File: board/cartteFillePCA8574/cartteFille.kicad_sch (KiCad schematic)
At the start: 13 parts, among them U1 LM358, U201 PCA8574D,518, U202 PCA8574D,518

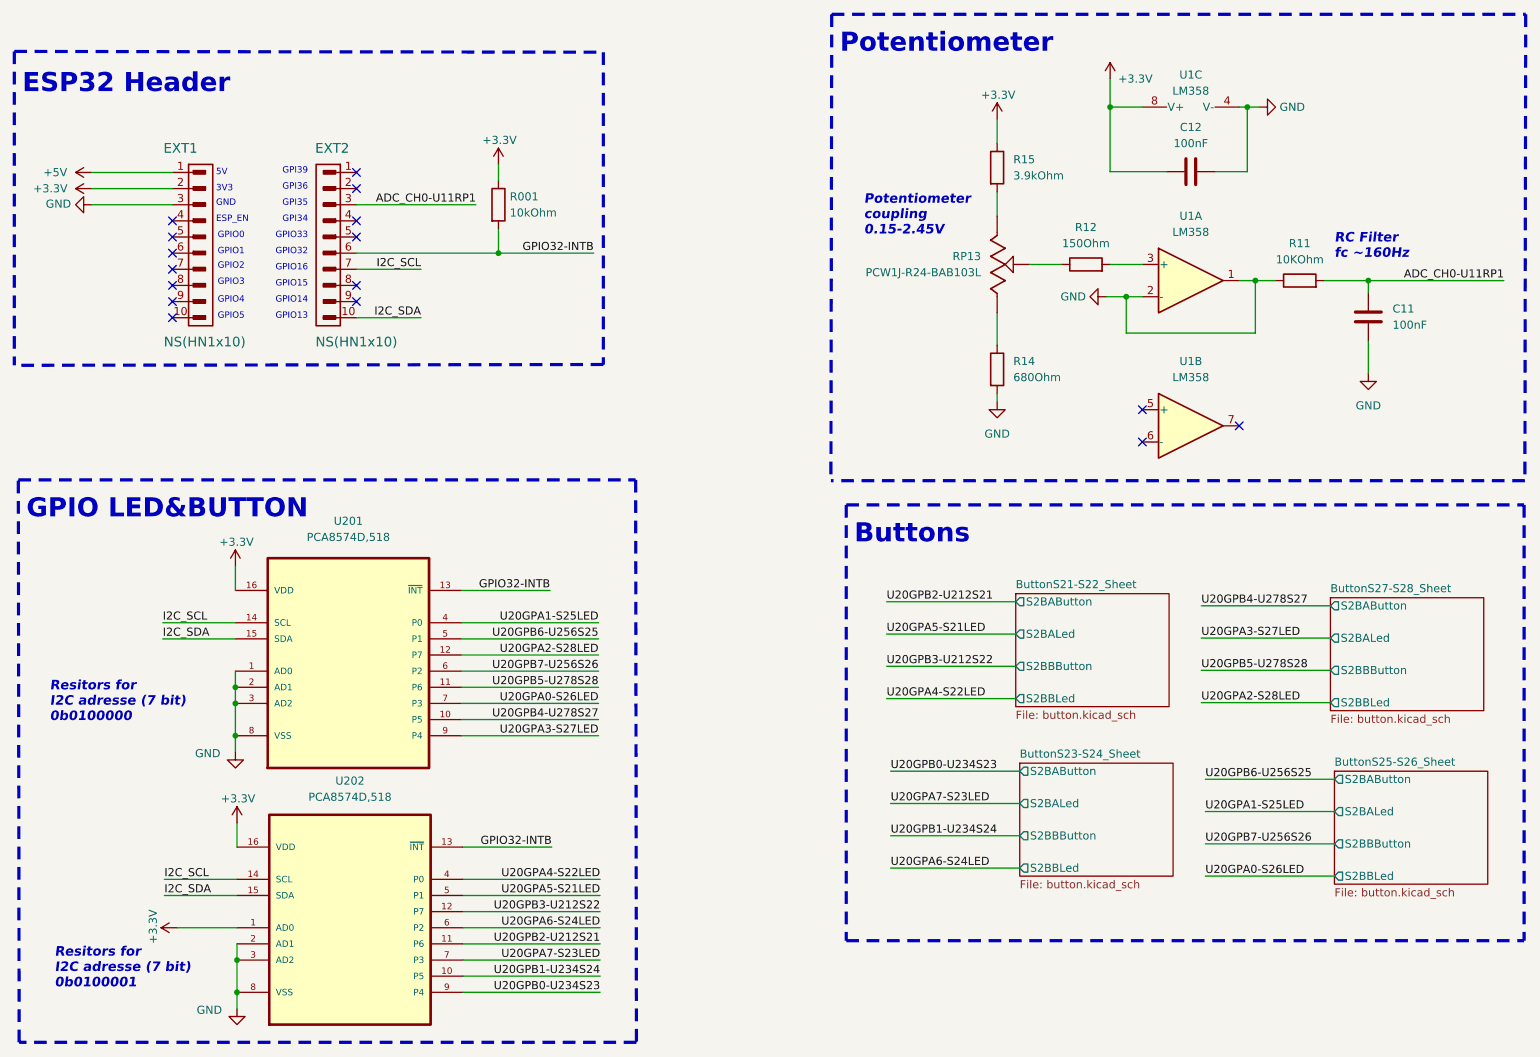
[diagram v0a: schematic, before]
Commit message: Review_GPIO_Replaced
version avant la review du pcb avec les nouveau gpio
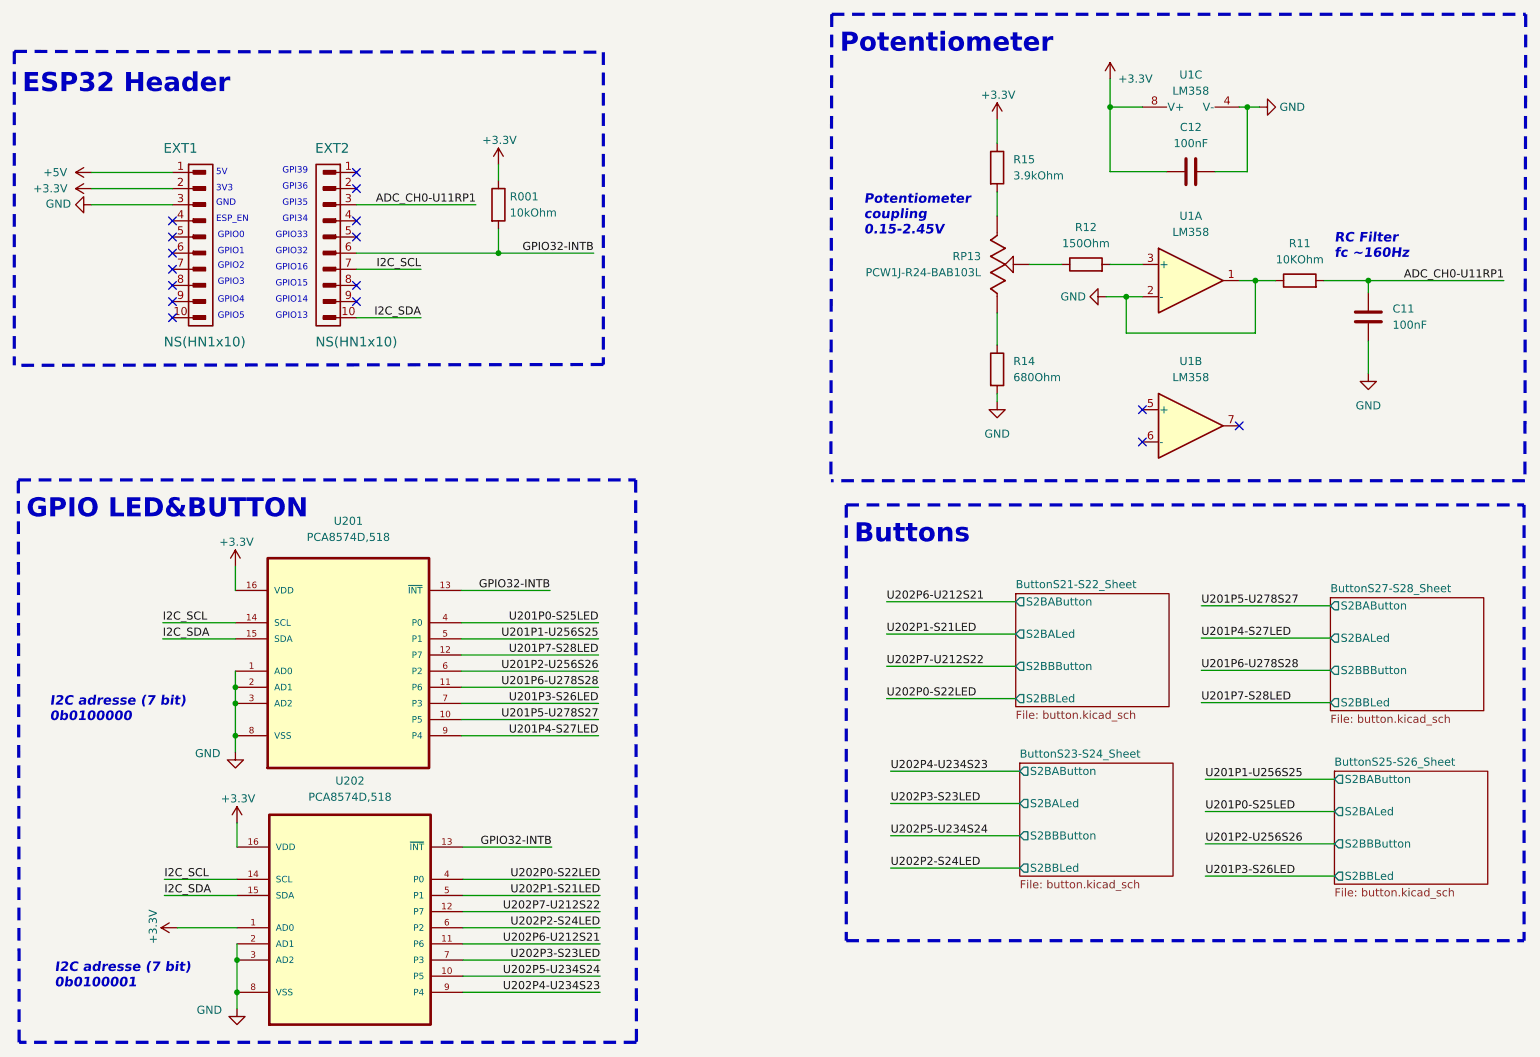
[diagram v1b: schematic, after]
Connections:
- net U20GPA0-S26LED renamed U201P3-S26LED
- net U20GPA1-S25LED renamed U201P0-S25LED
- net U20GPA2-S28LED renamed U201P7-S28LED
- net U20GPA3-S27LED renamed U201P4-S27LED
- net U20GPA4-S22LED renamed U202P0-S22LED
- net U20GPA5-S21LED renamed U202P1-S21LED
- net U20GPA6-S24LED renamed U202P2-S24LED
- net U20GPA7-S23LED renamed U202P3-S23LED
- net U20GPB0-U234S23 renamed U202P4-U234S23
- net U20GPB1-U234S24 renamed U202P5-U234S24
- net U20GPB2-U212S21 renamed U202P6-U212S21
- net U20GPB3-U212S22 renamed U202P7-U212S22
- net U20GPB4-U278S27 renamed U201P5-U278S27
- net U20GPB5-U278S28 renamed U201P6-U278S28
- net U20GPB6-U256S25 renamed U201P1-U256S25
- net U20GPB7-U256S26 renamed U201P2-U256S26
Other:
- note added: "I2C adresse (7 bit) 0b0100000"
- note added: "I2C adresse (7 bit) 0b0100001"
- note removed: "Resitors for I2C adresse (7 bit) 0b0100000"
- note removed: "Resitors for I2C adresse (7 bit) 0b0100001"
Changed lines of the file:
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@@
     (effects (font (size 3 3) (thickness 0.6) bold) (justify left bottom))
   )
-  (text "Resitors for\nI2C adresse (7 bit)\n0b0100000" (at 39.116 128.778 0)
+  (text "I2C adresse (7 bit)\n0b0100000" (at 39.116 128.778 0)
     (effects (font (size 1.5 1.5) (thickness 0.3) bold italic) (justify left bottom))
   )
@@
     (effects (font (size 1 1)) (justify left bottom))
   )
-  (text "Resitors for\nI2C adresse (7 bit)\n0b0100001" (at 39.878 170.688 0)
+  (text "I2C adresse (7 bit)\n0b0100001" (at 39.878 170.688 0)
     (effects (font (size 1.5 1.5) (thickness 0.3) bold italic) (justify left bottom))
   )
@@
     (effects (font (size 1 1)) (justify right bottom))
   )
-  (label "U20GPB5-U278S28" (at 125.476 123.19 180)
+  (label "U201P6-U278S28" (at 125.476 123.19 180)
     (effects (font (size 1.27 1.27)) (justify right bottom))
   )
@@
     (effects (font (size 1.27 1.27)) (justify right bottom))
   )
-  (label "U20GPB0-U234S23" (at 125.73 171.196 180)
+  (label "U202P4-U234S23" (at 125.73 171.196 180)
     (effects (font (size 1.27 1.27)) (justify right bottom))
   )
@@
     (effects (font (size 1.27 1.27)) (justify right bottom))
   )
-  (label "U20GPB7-U256S26" (at 220.98 147.828 0)
+  (label "U201P2-U256S26" (at 220.98 147.828 0)
     (effects (font (size 1.27 1.27)) (justify left bottom))
   )
@@
     (effects (font (size 1.27 1.27)) (justify right bottom))
   )
-  (label "U20GPA4-S22LED" (at 170.815 124.968 0)
+  (label "U202P0-S22LED" (at 170.815 124.968 0)
     (effects (font (size 1.27 1.27)) (justify left bottom))
   )
-  (label "U20GPB4-U278S27" (at 125.476 128.27 180)
+  (label "U201P5-U278S27" (at 125.476 128.27 180)
     (effects (font (size 1.27 1.27)) (justify right bottom))
   )
-  (label "U20GPB4-U278S27" (at 220.345 110.363 0)
+  (label "U201P5-U278S27" (at 220.345 110.363 0)
     (effects (font (size 1.27 1.27)) (justify left bottom))
   )
@@
     (effects (font (size 1.27 1.27)) (justify right bottom))
   )
-  (label "U20GPA7-S23LED" (at 171.45 141.478 0)
+  (label "U202P3-S23LED" (at 171.45 141.478 0)
     (effects (font (size 1.27 1.27)) (justify left bottom))
   )
-  (label "U20GPB1-U234S24" (at 125.73 168.656 180)
+  (label "U202P5-U234S24" (at 125.73 168.656 180)
     (effects (font (size 1.27 1.27)) (justify right bottom))
   )
-  (label "U20GPA1-S25LED" (at 125.476 113.03 180)
+  (label "U201P0-S25LED" (at 125.476 113.03 180)
     (effects (font (size 1.27 1.27)) (justify right bottom))
   )
@@
     (effects (font (size 1.27 1.27)) (justify left bottom))
   )
-  (label "U20GPB7-U256S26" (at 125.476 120.65 180)
+  (label "U201P2-U256S26" (at 125.476 120.65 180)
     (effects (font (size 1.27 1.27)) (justify right bottom))
   )
-  (label "U20GPB1-U234S24" (at 171.45 146.558 0)
+  (label "U202P5-U234S24" (at 171.45 146.558 0)
     (effects (font (size 1.27 1.27)) (justify left bottom))
   )
-  (label "U20GPA0-S26LED" (at 125.476 125.73 180)
+  (label "U201P3-S26LED" (at 125.476 125.73 180)
     (effects (font (size 1.27 1.27)) (justify right bottom))
   )
-  (label "U20GPB5-U278S28" (at 220.345 120.523 0)
+  (label "U201P6-U278S28" (at 220.345 120.523 0)
     (effects (font (size 1.27 1.27)) (justify left bottom))
   )
-  (label "U20GPA3-S27LED" (at 125.476 130.81 180)
+  (label "U201P4-S27LED" (at 125.476 130.81 180)
     (effects (font (size 1.27 1.27)) (justify right bottom))
   )
-  (label "U20GPA0-S26LED" (at 220.98 152.908 0)
+  (label "U201P3-S26LED" (at 220.98 152.908 0)
     (effects (font (size 1.27 1.27)) (justify left bottom))
   )
@@
     (effects (font (size 1.27 1.27)) (justify left bottom))
   )
-  (label "U20GPB6-U256S25" (at 220.98 137.668 0)
+  (label "U201P1-U256S25" (at 220.98 137.668 0)
     (effects (font (size 1.27 1.27)) (justify left bottom))
   )
-  (label "U20GPA7-S23LED" (at 125.73 166.116 180)
+  (label "U202P3-S23LED" (at 125.73 166.116 180)
     (effects (font (size 1.27 1.27)) (justify right bottom))
   )
-  (label "U20GPA2-S28LED" (at 220.345 125.603 0)
+  (label "U201P7-S28LED" (at 220.345 125.603 0)
     (effects (font (size 1.27 1.27)) (justify left bottom))
   )
-  (label "U20GPB6-U256S25" (at 125.476 115.57 180)
+  (label "U201P1-U256S25" (at 125.476 115.57 180)
     (effects (font (size 1.27 1.27)) (justify right bottom))
   )
-  (label "U20GPA1-S25LED" (at 220.98 142.748 0)
+  (label "U201P0-S25LED" (at 220.98 142.748 0)
     (effects (font (size 1.27 1.27)) (justify left bottom))
   )
-  (label "U20GPA5-S21LED" (at 170.815 114.808 0)
+  (label "U202P1-S21LED" (at 170.815 114.808 0)
     (effects (font (size 1.27 1.27)) (justify left bottom))
   )
-  (label "U20GPB3-U212S22" (at 125.73 158.496 180)
+  (label "U202P7-U212S22" (at 125.73 158.496 180)
     (effects (font (size 1.27 1.27)) (justify right bottom))
   )
-  (label "U20GPA6-S24LED" (at 125.73 161.036 180)
+  (label "U202P2-S24LED" (at 125.73 161.036 180)
     (effects (font (size 1.27 1.27)) (justify right bottom))
   )
-  (label "U20GPB0-U234S23" (at 171.45 136.398 0)
+  (label "U202P4-U234S23" (at 171.45 136.398 0)
     (effects (font (size 1.27 1.27)) (justify left bottom))
   )
-  (label "U20GPA6-S24LED" (at 171.45 151.638 0)
+  (label "U202P2-S24LED" (at 171.45 151.638 0)
     (effects (font (size 1.27 1.27)) (justify left bottom))
   )
-  (label "U20GPA5-S21LED" (at 125.73 155.956 180)
+  (label "U202P1-S21LED" (at 125.73 155.956 180)
     (effects (font (size 1.27 1.27)) (justify right bottom))
   )
@@
     (effects (font (size 1.27 1.27)) (justify left bottom))
   )
-  (label "U20GPB2-U212S21" (at 170.815 109.728 0)
+  (label "U202P6-U212S21" (at 170.815 109.728 0)
     (effects (font (size 1.27 1.27)) (justify left bottom))
   )
-  (label "U20GPB2-U212S21" (at 125.73 163.576 180)
+  (label "U202P6-U212S21" (at 125.73 163.576 180)
     (effects (font (size 1.27 1.27)) (justify right bottom))
   )
-  (label "U20GPB3-U212S22" (at 170.815 119.888 0)
+  (label "U202P7-U212S22" (at 170.815 119.888 0)
     (effects (font (size 1.27 1.27)) (justify left bottom))
   )
@@
     (effects (font (size 1.27 1.27)) (justify left bottom))
   )
-  (label "U20GPA3-S27LED" (at 220.345 115.443 0)
+  (label "U201P4-S27LED" (at 220.345 115.443 0)
     (effects (font (size 1.27 1.27)) (justify left bottom))
   )
-  (label "U20GPA4-S22LED" (at 125.73 153.416 180)
+  (label "U202P0-S22LED" (at 125.73 153.416 180)
     (effects (font (size 1.27 1.27)) (justify right bottom))
   )
-  (label "U20GPA2-S28LED" (at 125.476 118.11 180)
+  (label "U201P7-S28LED" (at 125.476 118.11 180)
     (effects (font (size 1.27 1.27)) (justify right bottom))
   )
